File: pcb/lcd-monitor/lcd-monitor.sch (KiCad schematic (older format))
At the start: 50 parts, among them J1 Conn_01x07_Male, J2 Conn_01x08_Male, J3 Conn_02x05_Odd_Even, J4 Screw_Terminal_01x02, J5 Conn_01x06_Male, SW1 SW_Push, U1 PC817, U10 AZ1117-3.3, U2 PC817, U3 PC817, U4 PC817, U5 PC817, U6 PC817, U7 PC817, U8 ATmega328PB-AU, U9 AZ1117-5.0, Y1 16MHz

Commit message: Remove unused CTS signal
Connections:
- net CTS: no longer names the net of J5.2 (Pin_2)
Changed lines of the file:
@@
 L power:GND #PWR031
 U 1 1 5BC9AAA7
-P 6750 1450
-F 0 "#PWR031" H 6750 1200 50  0001 C CNN
-F 1 "GND" H 6755 1277 50  0000 C CNN
-F 2 "" H 6750 1450 50  0001 C CNN
-F 3 "" H 6750 1450 50  0001 C CNN
-	1    6750 1450
+P 6750 1200
+F 0 "#PWR031" H 6750 950 50  0001 C CNN
+F 1 "GND" H 6755 1027 50  0000 C CNN
+F 2 "" H 6750 1200 50  0001 C CNN
+F 3 "" H 6750 1200 50  0001 C CNN
+	1    6750 1200
 	1    0    0    -1
 $EndComp
@@
 	1    0    0    -1
 $EndComp
-Text GLabel 10450 3250 2    50   Input ~ 0
-CTS
 Text GLabel 10450 3450 2    50   Input ~ 0
 328_RX
@@
 Key_8
 Wire Wire Line
-	6750 1150 6750 1450
+	6750 1150 6750 1200
 $Comp
 L power:GND #PWR032

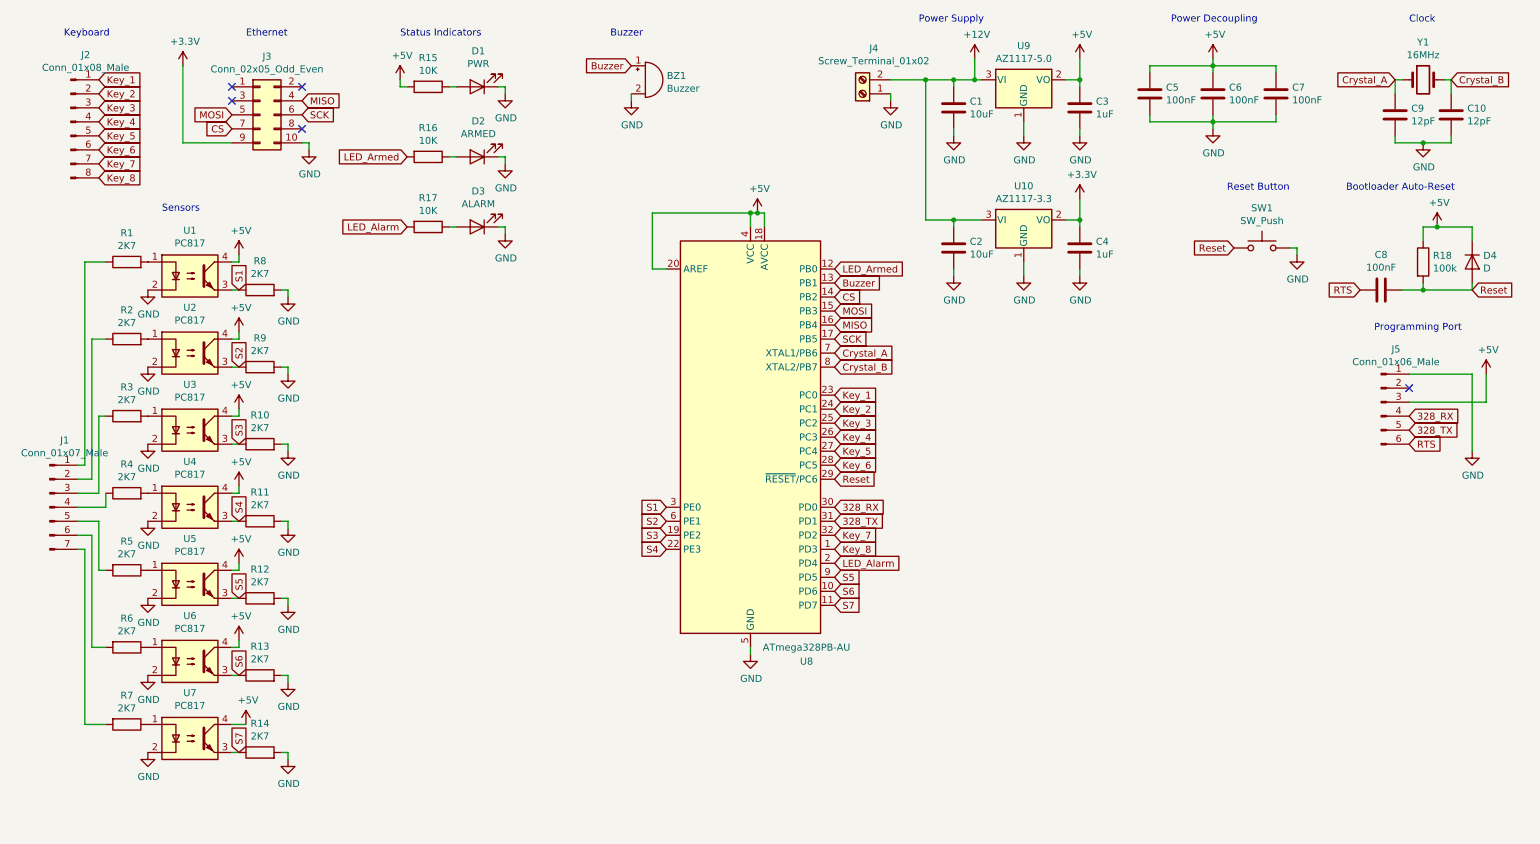
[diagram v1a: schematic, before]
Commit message: Add zone status led
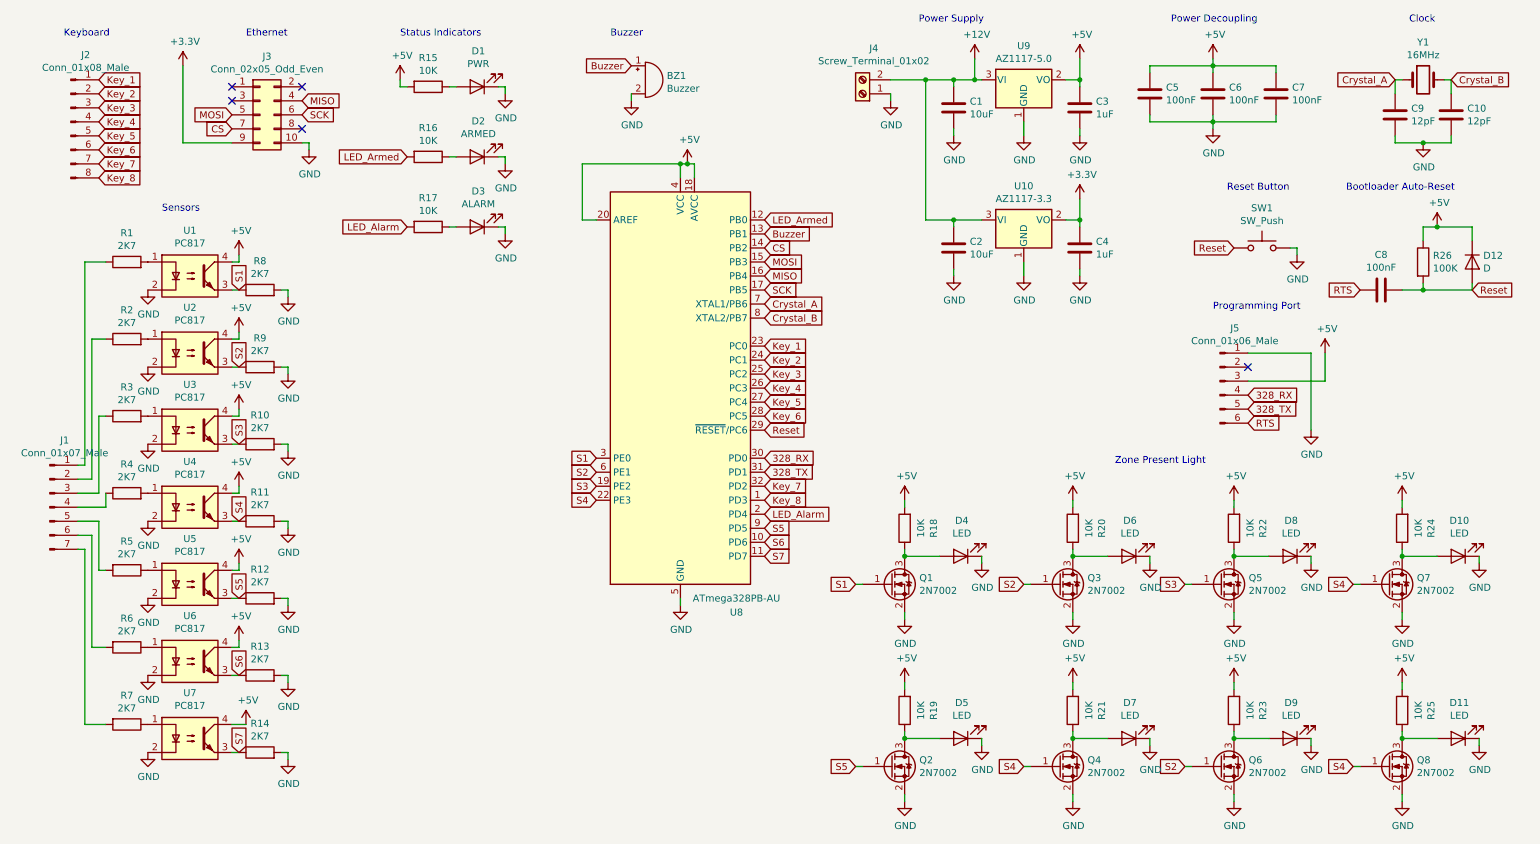
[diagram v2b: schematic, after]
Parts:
- added D10, D11, D4, D5, D6, D7, D8, D9: LED, LED_SMD:LED_0805_2012Metric, symbol Device:LED
- added Q1, Q2, Q3, Q4, Q5, Q6, Q7, Q8: 2N7002, Package_TO_SOT_SMD:SOT-23, symbol Transistor_FET:2N7002
- added R18, R19, R20, R21, R22, R23, R24, R25: 10K, Resistor_SMD:R_0805_2012Metric, symbol Device:R
- R26: renamed from R18; value 100k -> 100K
- renumbered D4 to D12
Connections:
- net +5V: now also R18.2, R19.2, R20.2, R21.2, R22.2, R23.2, R24.2, R25.2
- net GND: now also D10.1 (K), D11.1 (K), D4.1 (K), D5.1 (K), D6.1 (K), D7.1 (K), D8.1 (K), D9.1 (K), Q1.2 (S), Q2.2 (S), Q3.2 (S), Q4.2 (S), Q5.2 (S), Q6.2 (S), Q7.2 (S), Q8.2 (S)
- net S1: now also Q1.1 (G)
- net S2: now also Q3.1 (G), Q6.1 (G)
- net S3: now also Q5.1 (G)
- net S4: now also Q4.1 (G), Q7.1 (G), Q8.1 (G)
- net S5: now also Q2.1 (G)
- new net: D4.2 (A), Q1.3 (D), R18.1
- new net: D5.2 (A), Q2.3 (D), R19.1
- new net: D6.2 (A), Q3.3 (D), R20.1
- new net: D7.2 (A), Q4.3 (D), R21.1
- new net: D8.2 (A), Q5.3 (D), R22.1
- new net: D9.2 (A), Q6.3 (D), R23.1
- new net: D10.2 (A), Q7.3 (D), R24.1
- new net: D11.2 (A), Q8.3 (D), R25.1
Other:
- note added: "Zone Present Light"
- moved on the sheet: J5, U8

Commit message: Fix status LEDs
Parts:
- removed D11: LED, LED_SMD:LED_0805_2012Metric, symbol Device:LED
- removed Q8: 2N7002, Package_TO_SOT_SMD:SOT-23, symbol Transistor_FET:2N7002
- removed R25: 10K, Resistor_SMD:R_0805_2012Metric, symbol Device:R
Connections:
- net S2: no longer Q6.1 (G)
- net S4: no longer Q4.1 (G)
- net S6: now also Q4.1 (G)
- net S7: now also Q6.1 (G)
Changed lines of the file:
@@
 Connection ~ 8050 4450
 Text GLabel 7700 5950 0    50   Input ~ 0
-S4
+S6
 $Comp
 L Device:LED D7
@@
 Connection ~ 9200 4450
 Text GLabel 8850 5950 0    50   Input ~ 0
-S2
+S7
 $Comp
 L Device:LED D9
@@
 $EndComp
 Connection ~ 10400 4450
-Text GLabel 10050 5950 0    50   Input ~ 0
-S4
-$Comp
-L Device:LED D11
-U 1 1 5BE88BA1
-P 10800 5750
-F 0 "D11" H 10792 5495 50  0000 C CNN
-F 1 "LED" H 10792 5586 50  0000 C CNN
-F 2 "LED_SMD:LED_0805_2012Metric" H 10800 5750 50  0001 C CNN
-F 3 "~" H 10800 5750 50  0001 C CNN
-	1    10800 5750
-	-1   0    0    1
-$EndComp
-$Comp
-L Device:R R25
-U 1 1 5BE88BA7
-P 10400 5550
-F 0 "R25" V 10193 5550 50  0000 C CNN
-F 1 "10K" V 10284 5550 50  0000 C CNN
-F 2 "Resistor_SMD:R_0805_2012Metric" V 10330 5550 50  0001 C CNN
-F 3 "~" H 10400 5550 50  0001 C CNN
-	1    10400 5550
-	-1   0    0    1
-$EndComp
-$Comp
-L power:+5V #PWR066
-U 1 1 5BE88BAD
-P 10400 5350
-F 0 "#PWR066" H 10400 5200 50  0001 C CNN
-F 1 "+5V" H 10415 5523 50  0000 C CNN
-F 2 "" H 10400 5350 50  0001 C CNN
-F 3 "" H 10400 5350 50  0001 C CNN
-	1    10400 5350
-	1    0    0    -1
-$EndComp
-Wire Wire Line
-	10050 5950 10100 5950
-Wire Wire Line
-	10650 5750 10400 5750
-Wire Wire Line
-	10400 5750 10400 5700
-Wire Wire Line
-	10400 5400 10400 5350
-$Comp
-L power:GND #PWR067
-U 1 1 5BE88BB7
-P 10400 6200
-F 0 "#PWR067" H 10400 5950 50  0001 C CNN
-F 1 "GND" H 10405 6027 50  0000 C CNN
-F 2 "" H 10400 6200 50  0001 C CNN
-F 3 "" H 10400 6200 50  0001 C CNN
-	1    10400 6200
-	1    0    0    -1
-$EndComp
-$Comp
-L power:GND #PWR071
-U 1 1 5BE88BBD
-P 10950 5800
-F 0 "#PWR071" H 10950 5550 50  0001 C CNN
-F 1 "GND" H 10955 5627 50  0000 C CNN
-F 2 "" H 10950 5800 50  0001 C CNN
-F 3 "" H 10950 5800 50  0001 C CNN
-	1    10950 5800
-	1    0    0    -1
-$EndComp
-Wire Wire Line
-	10400 6200 10400 6150
-Wire Wire Line
-	10950 5800 10950 5750
-$Comp
-L Transistor_FET:2N7002 Q8
-U 1 1 5BE88BC5
-P 10300 5950
-F 0 "Q8" H 10505 5996 50  0000 L CNN
-F 1 "2N7002" H 10505 5905 50  0000 L CNN
-F 2 "Package_TO_SOT_SMD:SOT-23" H 10500 5875 50  0001 L CIN
-F 3 "https://www.fairchildsemi.com/datasheets/2N/2N7002.pdf" H 10300 5950 50  0001 L CNN
-	1    10300 5950
-	1    0    0    -1
-$EndComp
-Connection ~ 10400 5750
 $EndSCHEMATC
